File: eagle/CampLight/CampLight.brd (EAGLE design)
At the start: 63.5 x 63.5 mm, 27 parts, among them U1 ATMEGA328P_PDIP

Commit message: Latest Camplight work
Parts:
- removed IC1: (no value), SparkFun-PowerIC:TO-220-ALT
- removed U$1: DIODE-ZENERPTH, SparkFun-DiscreteSemi:DIODE-ZENER
- added D1: (no value), SparkFun-DiscreteSemi:DIODE-1N4001
- added LED7: (no value), SparkFun-LED:LED3MM
- added R8: (no value), SparkFun-Resistors:AXIAL-0.3
- added VREG: (no value), v-reg:78LXX
- moved C2 9.25 mm to (41.9, 2.54), turned to 270 degrees
- moved C1 5.68 mm to (41.9, 10.2), turned to 90 degrees
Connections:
- new net N$19: LED7.K, R8.P$2
- new net N$20: LED7.A, U1.6
- net 5V: now also VREG.OUT; no longer IC1.OUT
- net GND: now also R8.P$1, VREG.GND; no longer IC1.GND
- net N$1: now also D1.C, VREG.IN; no longer IC1.IN, U$1.P$1
- net N$5: now also D1.A; no longer U$1.P$2
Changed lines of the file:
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@@
 <element name="U1" library="SparkFun-DigitalIC" package="DIL28-3" value="ATMEGA328P_PDIP" x="31.75" y="31.75" rot="R90"/>
 <element name="Y1" library="SparkFun-FreqCtrl" package="RESONATOR-PTH" value="" x="31.75" y="8.89" rot="R180"/>
-<element name="IC1" library="SparkFun-PowerIC" package="TO-220-ALT" value="" x="48.26" y="8.89" rot="R296.5"/>
-<element name="C1" library="SparkFun-Passives" package="CPOL-RADIAL-10UF-25V" value="" x="39.37" y="5.08" rot="R270"/>
-<element name="C2" library="SparkFun-Passives" package="CPOL-RADIAL-10UF-25V" value="" x="39.37" y="11.43" rot="R90"/>
+<element name="VREG" library="v-reg" package="78LXX" value="" x="48.26" y="6.35" smashed="yes" rot="R270">
+<attribute name="NAME" x="51.435" y="8.255" size="1.27" layer="25" ratio="10" rot="R270"/>
+<attribute name="VALUE" x="46.99" y="3.175" size="1.27" layer="27" ratio="10" rot="R270"/>
+</element>
+<element name="C1" library="SparkFun-Passives" package="CPOL-RADIAL-10UF-25V" value="" x="41.91" y="10.16" rot="R90"/>
+<element name="C2" library="SparkFun-Passives" package="CPOL-RADIAL-10UF-25V" value="" x="41.91" y="2.54" rot="R270"/>
 <element name="C3" library="SparkFun-Passives" package="CAP-PTH-SMALL" value="" x="39.37" y="30.48" rot="R90"/>
 <element name="PWRIN" library="SparkFun-Passives" package="1X02_LOCK" value="" x="8.89" y="5.08" rot="R90"/>
@@
 <element name="R5" library="SparkFun-Resistors" package="AXIAL-0.3" value="" x="52.07" y="31.75" rot="R90"/>
 <element name="R6" library="SparkFun-Resistors" package="AXIAL-0.3" value="" x="49.53" y="43.18" rot="R90"/>
-<element name="U$1" library="SparkFun-DiscreteSemi" package="DIODE-ZENER" value="DIODE-ZENERPTH" x="25.4" y="5.08" rot="R180"/>
 <element name="Q1" library="SparkFun-DiscreteSemi" package="TO-92-AMMO" value="" x="31.75" y="54.61"/>
 <element name="POT" library="SparkFun-Passives" package="1X03" value="JUMPER-3PTH" x="13.97" y="55.88"/>
@@
 <element name="C4" library="SparkFun-Passives" package="CAP-PTH-SMALL" value="" x="6.35" y="13.97"/>
 <element name="R7" library="SparkFun-Passives" package="AXIAL-0.4" value="" x="31.75" y="59.69"/>
+<element name="LED7" library="SparkFun-LED" package="LED3MM" value="" x="24.13" y="31.75" rot="R90"/>
+<element name="R8" library="SparkFun-Resistors" package="AXIAL-0.3" value="" x="13.97" y="50.8"/>
+<element name="D1" library="SparkFun-DiscreteSemi" package="DIODE-1N4001" value="" x="21.59" y="11.43"/>
 </elements>
 <signals>
@@
 <contactref element="U1" pad="21"/>
 <contactref element="U1" pad="20"/>
-<contactref element="IC1" pad="OUT"/>
+<contactref element="VREG" pad="OUT"/>
 <contactref element="C1" pad="1"/>
 <contactref element="JP1" pad="P$4"/>
@@
 <contactref element="R3" pad="P$2"/>
 <contactref element="R2" pad="P$2"/>
-<wire x1="52.07" y1="27.94" x2="48.26" y2="24.13" width="0" layer="19" extent="1-1"/>
-<wire x1="49.53" y1="39.37" x2="52.07" y2="27.94" width="0" layer="19" extent="1-1"/>
-<wire x1="39.37" y1="30.48" x2="52.07" y2="27.94" width="0" layer="19" extent="1-1"/>
+<wire x1="52.07" y1="27.94" x2="49.53" y2="39.37" width="0" layer="19" extent="1-1"/>
+<wire x1="48.26" y1="24.13" x2="52.07" y2="27.94" width="0" layer="19" extent="1-1"/>
+<wire x1="39.37" y1="30.48" x2="48.26" y2="24.13" width="0" layer="19" extent="1-1"/>
 <wire x1="35.56" y1="30.48" x2="39.37" y2="30.48" width="0" layer="19" extent="1-1"/>
 <wire x1="27.94" y1="33.02" x2="35.56" y2="30.48" width="0" layer="19" extent="1-1"/>
 <wire x1="27.94" y1="35.56" x2="27.94" y2="33.02" width="0" layer="19" extent="1-1"/>
-<wire x1="39.37" y1="3.81" x2="49.53" y2="39.37" width="0" layer="19" extent="1-1"/>
-<wire x1="45.983640625" y1="4.91685" x2="39.37" y2="3.81" width="0" layer="19" extent="1-1"/>
-<wire x1="11.43" y1="35.56" x2="27.94" y2="35.56" width="0" layer="19" extent="1-1"/>
+<wire x1="41.91" y1="11.43" x2="48.26" y2="24.13" width="0" layer="19" extent="1-1"/>
+<wire x1="48.26" y1="7.62" x2="41.91" y2="11.43" width="0" layer="19" extent="1-1"/>
+<wire x1="15.24" y1="24.13" x2="27.94" y2="33.02" width="0" layer="19" extent="1-1"/>
+<wire x1="11.43" y1="35.56" x2="15.24" y2="24.13" width="0" layer="19" extent="1-1"/>
 <wire x1="6.35" y1="33.02" x2="11.43" y2="35.56" width="0" layer="19" extent="1-1"/>
-<wire x1="15.24" y1="24.13" x2="6.35" y2="33.02" width="0" layer="19" extent="1-1"/>
 <wire x1="15.24" y1="46.99" x2="11.43" y2="35.56" width="0" layer="19" extent="1-1"/>
 </signal>
@@
 <contactref element="C2" pad="2"/>
 <contactref element="C1" pad="2"/>
-<contactref element="IC1" pad="GND"/>
+<contactref element="VREG" pad="GND"/>
 <contactref element="PWRIN" pad="2"/>
 <contactref element="JP1" pad="P$6"/>
 <contactref element="Q1" pad="1"/>
+<contactref element="R8" pad="P$1"/>
 <wire x1="35.56" y1="33.02" x2="29.21" y2="54.61" width="0" layer="19" extent="1-1"/>
 <wire x1="39.37" y1="33.02" x2="35.56" y2="33.02" width="0" layer="19" extent="1-1"/>
 <wire x1="27.94" y1="30.48" x2="35.56" y2="33.02" width="0" layer="19" extent="1-1"/>
-<wire x1="39.37" y1="6.35" x2="39.37" y2="33.02" width="0" layer="19" extent="1-1"/>
-<wire x1="39.37" y1="10.16" x2="39.37" y2="6.35" width="0" layer="19" extent="1-1"/>
-<wire x1="44.8503" y1="7.189984375" x2="39.37" y2="6.35" width="0" layer="19" extent="1-1"/>
+<wire x1="41.91" y1="3.81" x2="39.37" y2="33.02" width="0" layer="19" extent="1-1"/>
+<wire x1="41.91" y1="8.89" x2="41.91" y2="3.81" width="0" layer="19" extent="1-1"/>
+<wire x1="50.165" y1="6.35" x2="41.91" y2="8.89" width="0" layer="19" extent="1-1"/>
 <wire x1="6.35" y1="38.1" x2="27.94" y2="30.48" width="0" layer="19" extent="1-1"/>
-<wire x1="8.89" y1="7.7978" x2="39.37" y2="10.16" width="0" layer="19" extent="1-1"/>
+<wire x1="8.89" y1="7.7978" x2="27.94" y2="30.48" width="0" layer="19" extent="1-1"/>
+<wire x1="10.16" y1="50.8" x2="8.89" y2="7.7978" width="0" layer="19" extent="1-1"/>
 </signal>
 <signal name="N$1">
-<contactref element="IC1" pad="IN"/>
+<contactref element="VREG" pad="IN"/>
 <contactref element="C2" pad="1"/>
-<contactref element="U$1" pad="P$1"/>
-<wire x1="39.37" y1="12.7" x2="43.71695625" y2="9.46311875" width="0" layer="19" extent="1-1"/>
-<wire x1="28.956" y1="5.08" x2="39.37" y2="12.7" width="0" layer="19" extent="1-1"/>
+<contactref element="D1" pad="C"/>
+<wire x1="41.91" y1="1.27" x2="48.26" y2="5.08" width="0" layer="19" extent="1-1"/>
+<wire x1="26.67" y1="11.43" x2="41.91" y2="1.27" width="0" layer="19" extent="1-1"/>
 </signal>
 <signal name="N$6">
@@
 <signal name="N$5">
 <contactref element="SWITCH" pad="2"/>
-<contactref element="U$1" pad="P$2"/>
-<wire x1="16.6878" y1="5.08" x2="21.844" y2="5.08" width="0" layer="19" extent="1-1"/>
+<contactref element="D1" pad="A"/>
+<wire x1="16.51" y1="11.43" x2="16.6878" y2="5.08" width="0" layer="19" extent="1-1"/>
 </signal>
 <signal name="N$12">
@@
 <wire x1="26.67" y1="59.69" x2="31.75" y2="54.61" width="0" layer="19" extent="1-1"/>
 </signal>
+<signal name="N$19">
+<contactref element="LED7" pad="K"/>
+<contactref element="R8" pad="P$2"/>
+<wire x1="17.78" y1="50.8" x2="24.13" y2="33.02" width="0" layer="19" extent="1-1"/>
+</signal>
+<signal name="N$20">
+<contactref element="LED7" pad="A"/>
+<contactref element="U1" pad="6"/>
+<wire x1="24.13" y1="30.48" x2="35.56" y2="27.94" width="0" layer="19" extent="1-1"/>
+</signal>
 </signals>

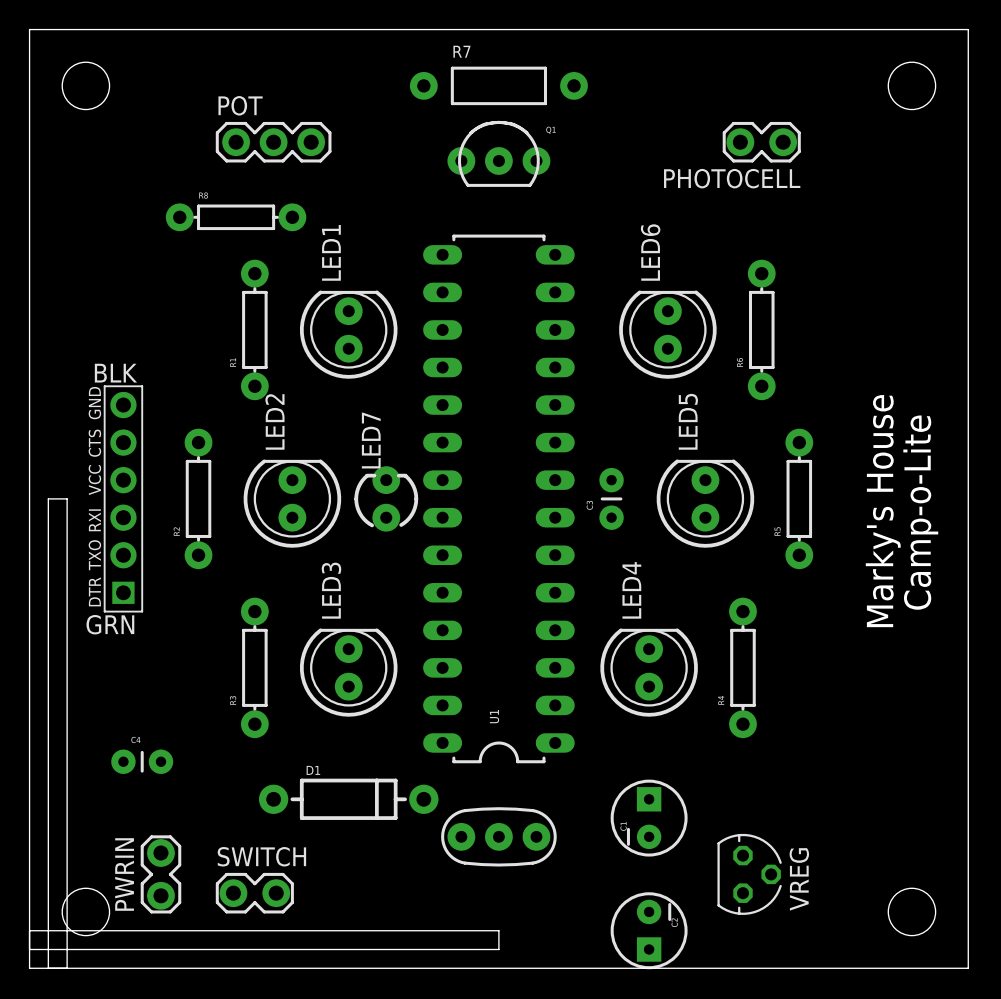
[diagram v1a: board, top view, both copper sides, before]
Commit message: Update eagle files with touch switch
This is a final release candidate. I have sent this board to Osh Park (oshpark.com) for fabrication.
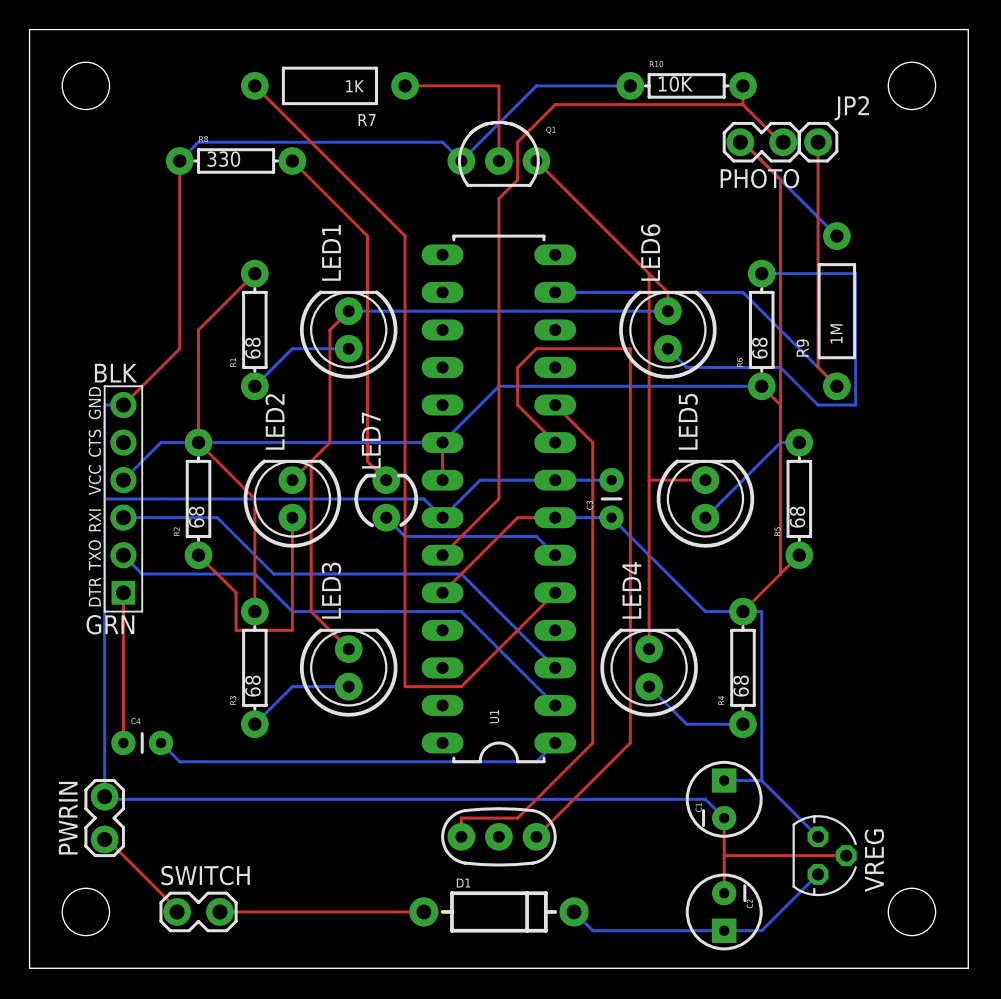
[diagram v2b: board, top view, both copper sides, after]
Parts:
- removed POT: JUMPER-3PTH, SparkFun-Passives:1X03
- added JP2: TOUCH, SparkFun-Connectors:1X01
- added R10: 10K, SparkFun-Resistors:AXIAL-0.3
- added R9: 1M, SparkFun-Passives:AXIAL-0.4
- C1: value (none) -> 10uF
- C2: value (none) -> 100uF
- C3, C4: value (none) -> 0.1mF
- R1, R2, R3, R4, R5, R6: value (none) -> 68
- R7: value (none) -> 1K
- R8: value (none) -> 330
- moved D1 12.7 mm to (31.8, 3.81)
- moved R7 11.4 mm to (20.3, 59.7), turned to 180 degrees
- moved PWRIN 5.39 mm to (5.08, 8.89)
- moved VREG 5.24 mm to (53.3, 7.62)
- moved C1 5.24 mm to (47.0, 11.4)
- moved C2 5.24 mm to (47.0, 3.81)
- moved SWITCH 4.02 mm to (10.2, 3.81)
- moved R8 3.81 mm to (14.0, 54.6)
- moved C4 1.27 mm to (6.35, 15.2)
- renumbered PHOTOCELL to PHOTO
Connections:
- new net N$21: JP2.1, R9.P$1, U1.13
- new net N$24: PHOTO.1, R10.P$2, U1.23
- net 5V: now also PHOTO.2, R9.P$2, U1.24
- net GND: now also R10.P$1
- net N$7: now also LED3.K
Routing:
- net GND: track 0.00 -> 171.3 mm
- net 5V: track 0.00 -> 166.8 mm
- net N$7: track 0.00 -> 91.4 mm
- net N$6: track 0.00 -> 57.6 mm
- net N$24: track 0.00 -> 51.4 mm
- net N$3: track 0.00 -> 49.9 mm
- net N$21: track 0.00 -> 38.7 mm
- net N$4: track 0.00 -> 36.2 mm
- net N$15: track 0.00 -> 33.4 mm
- net N$12: track 0.00 -> 33.4 mm
- net N$11: track 0.00 -> 29.5 mm
- net N$16: track 0.00 -> 27.7 mm
- net N$19: track 0.00 -> 24.2 mm
- net N$1: track 0.00 -> 18.6 mm
- net N$13: track 0.00 -> 17.6 mm
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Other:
- outline, holes or cut-outs redrawn
- board text removed: "Camp-o-Lite"
- board text removed: "Marky's House"

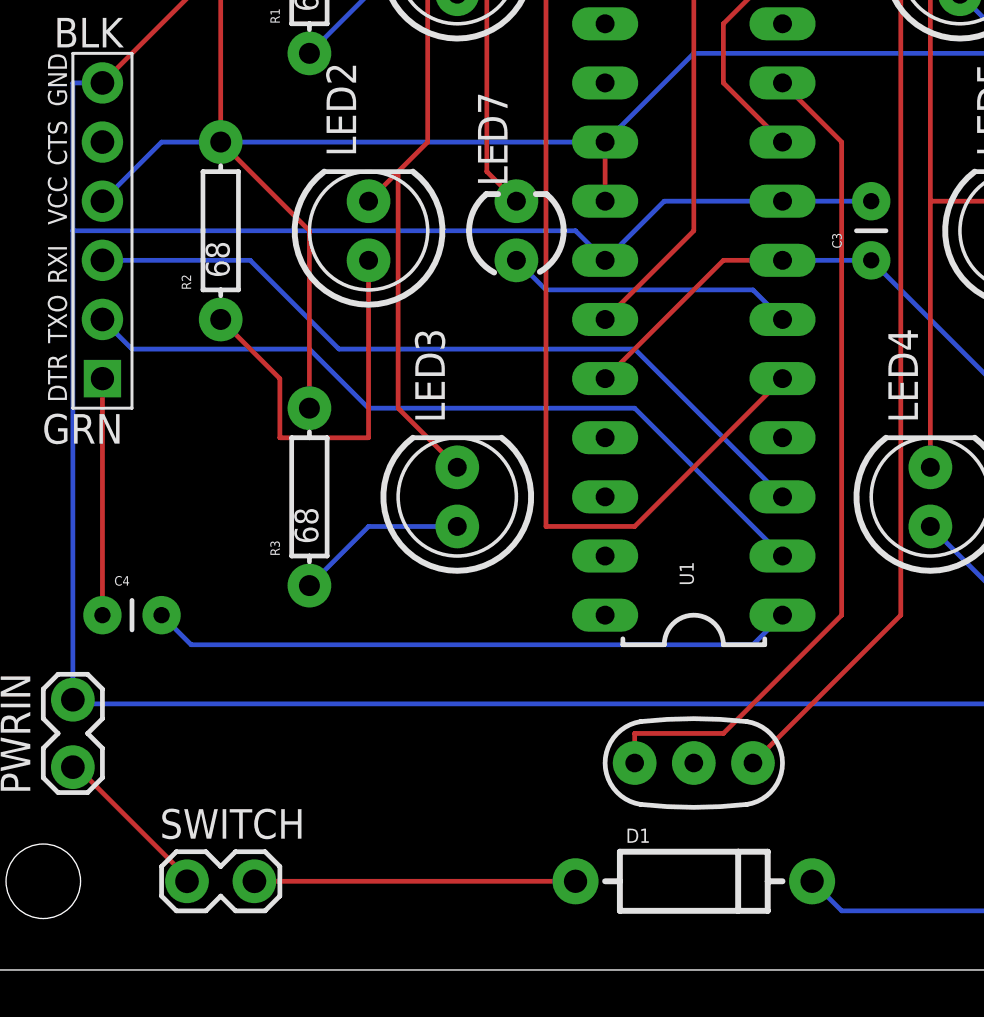
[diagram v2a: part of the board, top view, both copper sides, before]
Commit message: Update camplight eagle files * Add pull up resistor to reset pin * reverse R & T on programming header
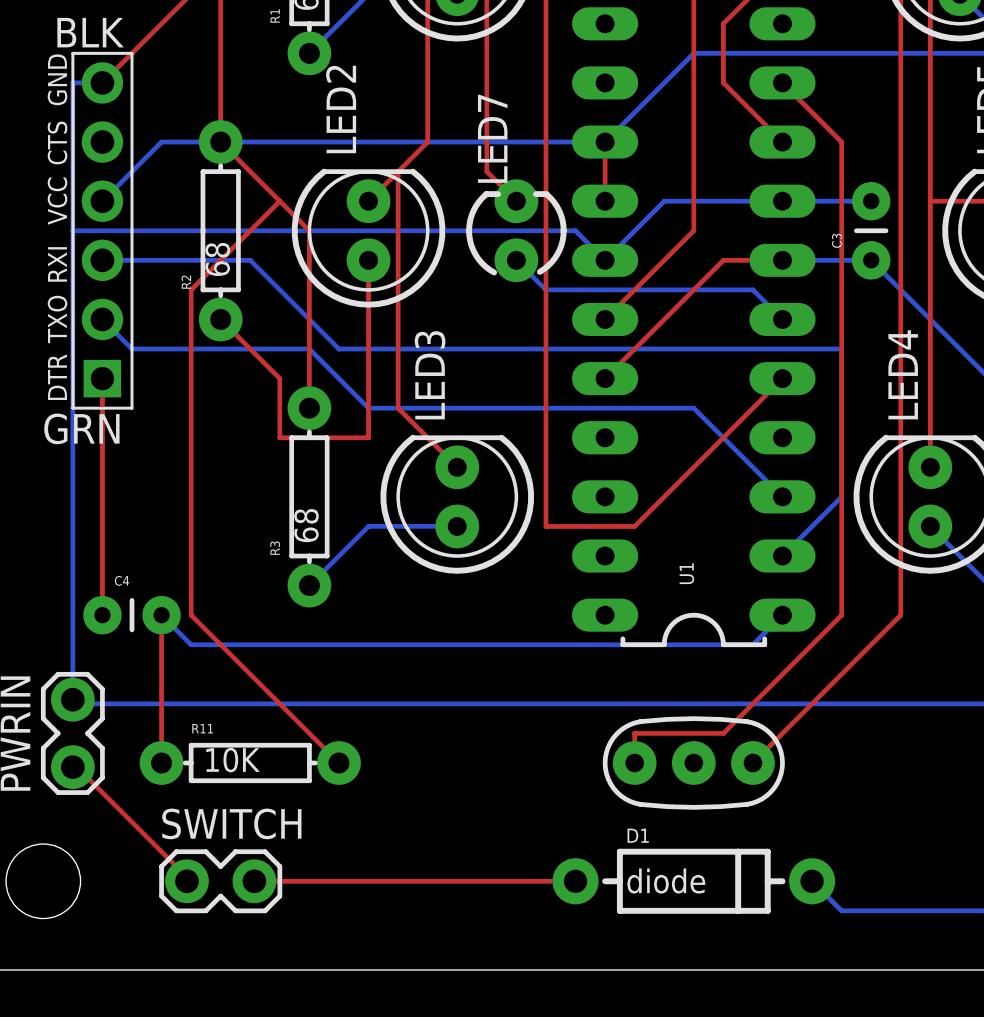
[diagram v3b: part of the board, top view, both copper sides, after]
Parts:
- added R11: 10K, SparkFun-Resistors:AXIAL-0.3
- D1: value (none) -> diode
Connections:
- net 5V: now also R11.P$2
- net N$12: now also U1.2; no longer U1.3
- net N$15: now also U1.3; no longer U1.2
- net N$16: now also R11.P$1
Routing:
- net 5V: track 166.8 -> 195.2 mm
- net N$12: track 33.4 -> 43.3 mm
- net N$16: track 27.7 -> 34.1 mm
- net N$15: track 33.4 -> 32.4 mm
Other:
- board text added: "Camp-o-Light R1.1"
- board text added: "Marky's House"
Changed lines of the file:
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@@
 <hole x="59.69" y="3.81" drill="3.2"/>
 <hole x="3.81" y="3.81" drill="3.2"/>
+<text x="57.15" y="13.97" size="1.778" layer="51" rot="R90">Marky's House</text>
+<text x="60.96" y="13.97" size="1.778" layer="51" rot="R90">Camp-o-Light R1.1</text>
 </plain>
 <attributes>
@@
 <element name="LED7" library="SparkFun-LED" package="LED3MM" value="" x="24.13" y="31.75" rot="R90"/>
 <element name="R8" library="SparkFun-Resistors" package="AXIAL-0.3" value="330" x="13.97" y="54.61"/>
-<element name="D1" library="SparkFun-DiscreteSemi" package="DIODE-1N4001" value="" x="31.75" y="3.81"/>
+<element name="D1" library="SparkFun-DiscreteSemi" package="DIODE-1N4001" value="diode" x="31.75" y="3.81"/>
 <element name="R9" library="SparkFun-Passives" package="AXIAL-0.4" value="1M" x="54.61" y="44.45" rot="R90"/>
 <element name="JP2" library="SparkFun-Connectors" package="1X01" value="TOUCH" x="53.34" y="55.88"/>
 <element name="R10" library="SparkFun-Resistors" package="AXIAL-0.3" value="10K" x="44.45" y="59.69"/>
+<element name="R11" library="SparkFun-Resistors" package="AXIAL-0.3" value="10K" x="12.7" y="8.89"/>
 </elements>
 <signals>
@@
 <wire x1="11.43" y1="35.56" x2="27.94" y2="35.56" width="0.2032" layer="16"/>
 <wire x1="15.24" y1="31.75" x2="15.24" y2="24.13" width="0.2032" layer="1"/>
-<wire x1="11.43" y1="35.56" x2="15.24" y2="31.75" width="0.2032" layer="1"/>
+<wire x1="11.43" y1="35.56" x2="13.97" y2="33.02" width="0.2032" layer="1"/>
+<wire x1="13.97" y1="33.02" x2="15.24" y2="31.75" width="0.2032" layer="1"/>
 <wire x1="11.43" y1="43.18" x2="15.24" y2="46.99" width="0.2032" layer="1"/>
 <wire x1="11.43" y1="35.56" x2="11.43" y2="43.18" width="0.2032" layer="1"/>
@@
 <wire x1="35.56" y1="30.48" x2="33.02" y2="30.48" width="0.2032" layer="1"/>
 <wire x1="8.89" y1="35.56" x2="6.35" y2="33.02" width="0.2032" layer="16"/>
+<contactref element="R11" pad="P$2"/>
+<wire x1="10.16" y1="15.24" x2="16.51" y2="8.89" width="0.2032" layer="1"/>
+<wire x1="10.16" y1="29.21" x2="10.16" y2="15.24" width="0.2032" layer="1"/>
+<wire x1="13.97" y1="33.02" x2="10.16" y2="29.21" width="0.2032" layer="1"/>
 </signal>
 <signal name="GND">
@@
 </signal>
 <signal name="N$12">
-<contactref element="U1" pad="3"/>
 <contactref element="JP1" pad="P$3"/>
-<wire x1="29.21" y1="26.67" x2="35.56" y2="20.32" width="0.2032" layer="16"/>
-<wire x1="16.51" y1="26.67" x2="29.21" y2="26.67" width="0.2032" layer="16"/>
+<wire x1="16.51" y1="26.67" x2="38.1" y2="26.67" width="0.2032" layer="16"/>
 <wire x1="12.7" y1="30.48" x2="16.51" y2="26.67" width="0.2032" layer="16"/>
 <wire x1="6.35" y1="30.48" x2="12.7" y2="30.48" width="0.2032" layer="16"/>
+<contactref element="U1" pad="2"/>
+<wire x1="38.1" y1="20.32" x2="35.56" y2="17.78" width="0.2032" layer="16"/>
+<wire x1="38.1" y1="26.67" x2="38.1" y2="20.32" width="0.2032" layer="16"/>
 </signal>
 <signal name="N$15">
 <contactref element="JP1" pad="P$2"/>
-<contactref element="U1" pad="2"/>
-<wire x1="29.21" y1="24.13" x2="35.56" y2="17.78" width="0.2032" layer="16"/>
-<wire x1="17.78" y1="24.13" x2="29.21" y2="24.13" width="0.2032" layer="16"/>
+<wire x1="17.78" y1="24.13" x2="31.75" y2="24.13" width="0.2032" layer="16"/>
 <wire x1="15.24" y1="26.67" x2="17.78" y2="24.13" width="0.2032" layer="16"/>
 <wire x1="7.62" y1="26.67" x2="15.24" y2="26.67" width="0.2032" layer="16"/>
 <wire x1="6.35" y1="27.94" x2="7.62" y2="26.67" width="0.2032" layer="16"/>
+<contactref element="U1" pad="3"/>
+<wire x1="31.75" y1="24.13" x2="35.56" y2="20.32" width="0.2032" layer="16"/>
 </signal>
 <signal name="N$16">
@@
 <wire x1="10.16" y1="13.97" x2="34.29" y2="13.97" width="0.2032" layer="16"/>
 <wire x1="8.89" y1="15.24" x2="10.16" y2="13.97" width="0.2032" layer="16"/>
+<contactref element="R11" pad="P$1"/>
+<wire x1="8.89" y1="15.24" x2="8.89" y2="8.89" width="0.2032" layer="1"/>
 </signal>
 <signal name="N$17">
